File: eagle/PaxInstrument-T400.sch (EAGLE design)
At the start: 122 parts, among them IC1 MCP3424, U1 MCP9800, U3 MCP73831, U4 MIC5219-3.3V, U7 USD-SOCKETNEW, U8 NC7S32, X2 FH12-12S-0.5SH, Y1 RESONATORSMD

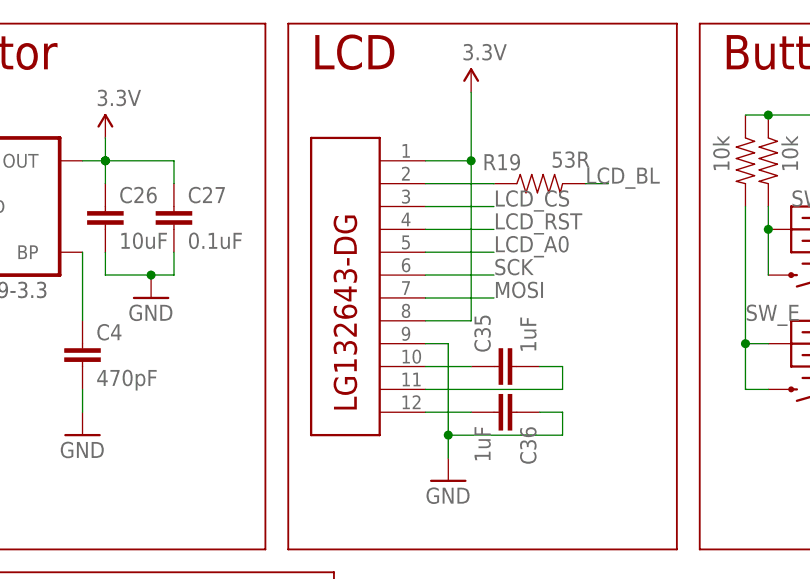
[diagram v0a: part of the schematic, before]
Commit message: - Moved switches a little
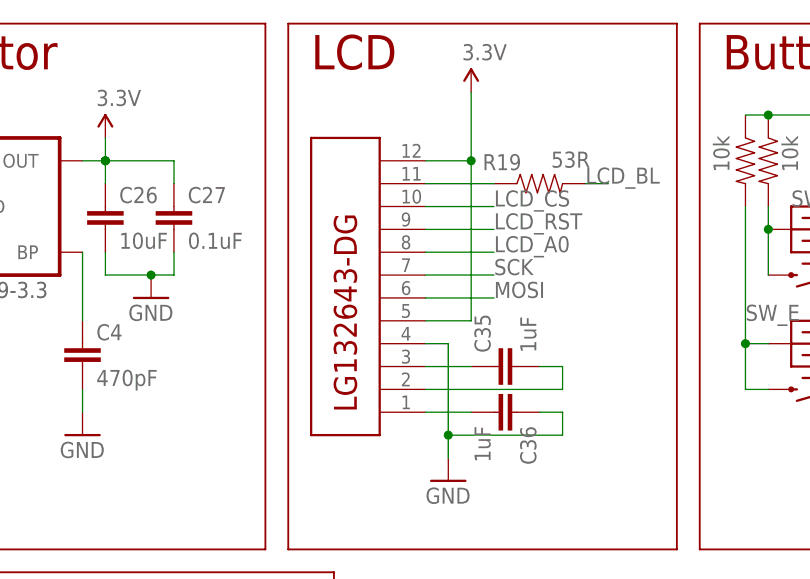
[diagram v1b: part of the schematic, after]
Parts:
- removed X2: FH12-12S-0.5SH, charlespax:FH12-12S-0.5SH
- added X1: FH12-12S-0.5SH, charlespax:FH12-12S-0.5SH
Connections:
- net 3.3V: now also X1.P$12, X1.P$5; no longer X2.P$1, X2.P$8
- net GND: now also X1.P$4; no longer X2.P$9
- net LCD_A0: now also X1.P$8; no longer X2.P$5
- net LCD_CS: now also X1.P$10; no longer X2.P$3
- net LCD_RST: now also X1.P$9; no longer X2.P$4
- net MOSI: now also X1.P$6; no longer X2.P$7
- net N$37: now also X1.P$3; no longer X2.P$10
- net N$38: now also X1.P$2; no longer X2.P$11
- net N$39: now also X1.P$1; no longer X2.P$12
- net N$4: now also X1.P$11; no longer X2.P$2
- net SCK: now also X1.P$7; no longer X2.P$6
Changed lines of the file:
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@@
 </part>
 <part name="GND17" library="SparkFun-Aesthetics" deviceset="GND" device=""/>
-<part name="X2" library="charlespax" deviceset="FH12-12S-0.5S" device="H">
-<attribute name="OC_DIGIKEY" value="HFJ112TR-ND"/>
-</part>
 <part name="P+4" library="SparkFun" deviceset="3.3V" device=""/>
 <part name="R19" library="SparkFun-Passives" deviceset="RESISTOR" device="0805-RES" value="53R"/>
@@
 <part name="GND20" library="SparkFun-Aesthetics" deviceset="GND" device=""/>
 <part name="P+8" library="SparkFun" deviceset="3.3V" device=""/>
+<part name="X1" library="charlespax" deviceset="FH12-12S-0.5S" device="H">
+<attribute name="OC_DIGIKEY" value="HFJ112TR-ND"/>
+</part>
 </parts>
 <sheets>
@@
 </instance>
 <instance part="GND17" gate="1" x="304.8" y="203.2"/>
-<instance part="X2" gate="G$1" x="297.18" y="210.82">
-<attribute name="OC_DIGIKEY" x="297.18" y="210.82" size="1.778" layer="96" display="off"/>
-</instance>
 <instance part="P+4" gate="G$1" x="307.34" y="246.38"/>
 <instance part="R19" gate="G$1" x="314.96" y="236.22" smashed="yes">
@@
 <instance part="GND20" gate="1" x="226.06" y="160.02"/>
 <instance part="P+8" gate="G$1" x="215.9" y="185.42"/>
+<instance part="X1" gate="G$1" x="297.18" y="238.76" rot="MR180">
+<attribute name="OC_DIGIKEY" x="297.18" y="238.76" size="1.778" layer="96" rot="MR180" display="off"/>
+</instance>
 </instances>
 <busses>
@@
 </segment>
 <segment>
-<pinref part="X2" gate="G$1" pin="P$8"/>
 <pinref part="P+4" gate="G$1" pin="3.3V"/>
 <wire x1="302.26" y1="220.98" x2="307.34" y2="220.98" width="0.1524" layer="91"/>
 <wire x1="307.34" y1="220.98" x2="307.34" y2="238.76" width="0.1524" layer="91"/>
-<pinref part="X2" gate="G$1" pin="P$1"/>
 <wire x1="307.34" y1="238.76" x2="307.34" y2="246.38" width="0.1524" layer="91"/>
 <wire x1="302.26" y1="238.76" x2="307.34" y2="238.76" width="0.1524" layer="91"/>
 <junction x="307.34" y="238.76"/>
+<pinref part="X1" gate="G$1" pin="P$5"/>
+<pinref part="X1" gate="G$1" pin="P$12"/>
 </segment>
 <segment>
@@
 <segment>
 <pinref part="GND17" gate="1" pin="GND"/>
-<pinref part="X2" gate="G$1" pin="P$9"/>
 <wire x1="304.8" y1="218.44" x2="304.8" y2="208.28" width="0.1524" layer="91"/>
 <wire x1="304.8" y1="208.28" x2="304.8" y2="205.74" width="0.1524" layer="91"/>
@@
 <wire x1="317.5" y1="208.28" x2="304.8" y2="208.28" width="0.1524" layer="91"/>
 <junction x="304.8" y="208.28"/>
+<pinref part="X1" gate="G$1" pin="P$4"/>
 </segment>
 <segment>
@@
 </segment>
 <segment>
-<pinref part="X2" gate="G$1" pin="P$7"/>
 <wire x1="302.26" y1="223.52" x2="309.88" y2="223.52" width="0.1524" layer="91"/>
 <label x="309.88" y="223.52" size="1.778" layer="95"/>
+<pinref part="X1" gate="G$1" pin="P$6"/>
 </segment>
 <segment>
@@
 </segment>
 <segment>
-<pinref part="X2" gate="G$1" pin="P$6"/>
 <wire x1="302.26" y1="226.06" x2="309.88" y2="226.06" width="0.1524" layer="91"/>
 <label x="309.88" y="226.06" size="1.778" layer="95"/>
+<pinref part="X1" gate="G$1" pin="P$7"/>
 </segment>
 <segment>
@@
 <net name="LCD_A0" class="0">
 <segment>
-<pinref part="X2" gate="G$1" pin="P$5"/>
 <wire x1="302.26" y1="228.6" x2="309.88" y2="228.6" width="0.1524" layer="91"/>
 <label x="309.88" y="228.6" size="1.778" layer="95"/>
+<pinref part="X1" gate="G$1" pin="P$8"/>
 </segment>
 <segment>
@@
 <net name="LCD_CS" class="0">
 <segment>
-<pinref part="X2" gate="G$1" pin="P$3"/>
 <wire x1="302.26" y1="233.68" x2="309.88" y2="233.68" width="0.1524" layer="91"/>
 <label x="309.88" y="233.68" size="1.778" layer="95"/>
+<pinref part="X1" gate="G$1" pin="P$10"/>
 </segment>
 <segment>
@@
 <net name="LCD_RST" class="0">
 <segment>
-<pinref part="X2" gate="G$1" pin="P$4"/>
 <wire x1="302.26" y1="231.14" x2="309.88" y2="231.14" width="0.1524" layer="91"/>
 <label x="309.88" y="231.14" size="1.778" layer="95"/>
+<pinref part="X1" gate="G$1" pin="P$9"/>
 </segment>
 <segment>
@@
 <net name="N$37" class="0">
 <segment>
-<pinref part="X2" gate="G$1" pin="P$10"/>
 <wire x1="302.26" y1="215.9" x2="307.34" y2="215.9" width="0.1524" layer="91"/>
 <pinref part="C35" gate="G$1" pin="1"/>
+<pinref part="X1" gate="G$1" pin="P$3"/>
 </segment>
 </net>
 <net name="N$38" class="0">
 <segment>
-<pinref part="X2" gate="G$1" pin="P$11"/>
 <pinref part="C35" gate="G$1" pin="2"/>
 <wire x1="314.96" y1="215.9" x2="317.5" y2="215.9" width="0.1524" layer="91"/>
 <wire x1="317.5" y1="215.9" x2="317.5" y2="213.36" width="0.1524" layer="91"/>
 <wire x1="317.5" y1="213.36" x2="302.26" y2="213.36" width="0.1524" layer="91"/>
+<pinref part="X1" gate="G$1" pin="P$2"/>
 </segment>
 </net>
 <net name="N$39" class="0">
 <segment>
-<pinref part="X2" gate="G$1" pin="P$12"/>
 <wire x1="302.26" y1="210.82" x2="307.34" y2="210.82" width="0.1524" layer="91"/>
 <pinref part="C36" gate="G$1" pin="2"/>
+<pinref part="X1" gate="G$1" pin="P$1"/>
 </segment>
 </net>
@@
 <net name="N$4" class="0">
 <segment>
-<pinref part="X2" gate="G$1" pin="P$2"/>
 <pinref part="R19" gate="G$1" pin="1"/>
 <wire x1="302.26" y1="236.22" x2="309.88" y2="236.22" width="0.1524" layer="91"/>
-</segment>
-</net>
+<pinref part="X1" gate="G$1" pin="P$11"/>
+</segment>
+</net>

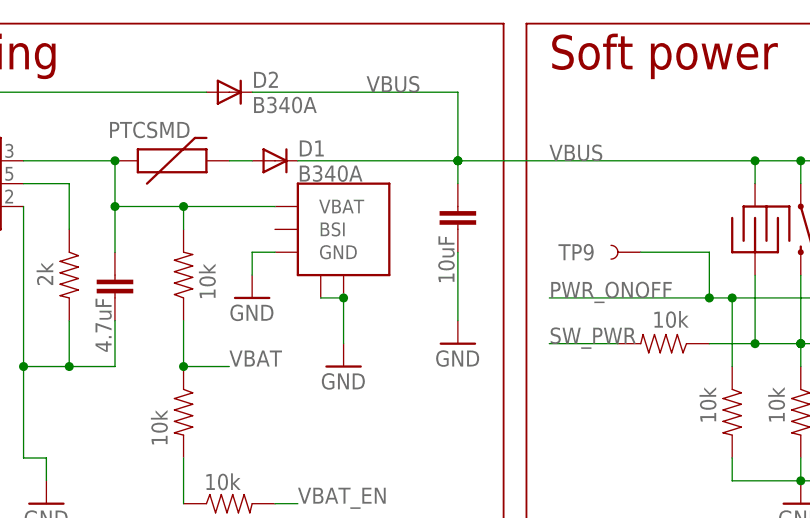
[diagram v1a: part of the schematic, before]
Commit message: - Still laying out board
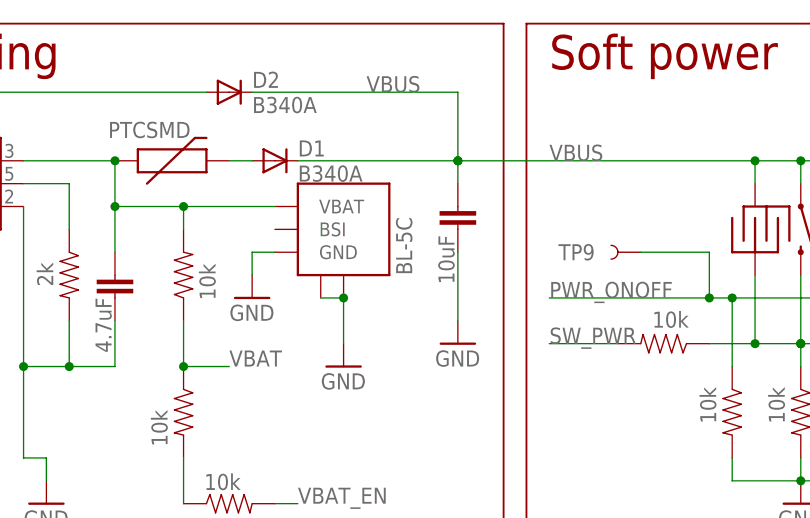
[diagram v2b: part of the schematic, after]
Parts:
- added U$6: BL-5C-OUTLINE, charlespax:BL-5C-OUTLINE
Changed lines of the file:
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@@
 <grid distance="0.1" unitdist="inch" unit="inch" style="lines" multiple="1" display="no" altdistance="0.01" altunitdist="inch" altunit="inch"/>
 <layers>
-<layer number="1" name="Top" color="4" fill="1" visible="no" active="no"/>
-<layer number="2" name="Route2" color="1" fill="3" visible="no" active="no"/>
-<layer number="3" name="Route3" color="4" fill="3" visible="no" active="no"/>
-<layer number="14" name="Route14" color="1" fill="6" visible="no" active="no"/>
-<layer number="15" name="Route15" color="4" fill="6" visible="no" active="no"/>
-<layer number="16" name="Bottom" color="1" fill="1" visible="no" active="no"/>
-<layer number="17" name="Pads" color="2" fill="1" visible="no" active="no"/>
-<layer number="18" name="Vias" color="2" fill="1" visible="no" active="no"/>
-<layer number="19" name="Unrouted" color="6" fill="1" visible="no" active="no"/>
-<layer number="20" name="Dimension" color="15" fill="1" visible="no" active="no"/>
-<layer number="21" name="tPlace" color="16" fill="1" visible="no" active="no"/>
-<layer number="22" name="bPlace" color="14" fill="1" visible="no" active="no"/>
-<layer number="23" name="tOrigins" color="15" fill="1" visible="no" active="no"/>
-<layer number="24" name="bOrigins" color="15" fill="1" visible="no" active="no"/>
-<layer number="25" name="tNames" color="7" fill="1" visible="no" active="no"/>
-<layer number="26" name="bNames" color="7" fill="1" visible="no" active="no"/>
-<layer number="27" name="tValues" color="7" fill="1" visible="no" active="no"/>
-<layer number="28" name="bValues" color="7" fill="1" visible="no" active="no"/>
+<layer number="1" name="Top" color="4" fill="1" visible="yes" active="no"/>
+<layer number="2" name="Route2" color="1" fill="3" visible="yes" active="no"/>
+<layer number="3" name="Route3" color="4" fill="3" visible="yes" active="no"/>
+<layer number="14" name="Route14" color="1" fill="6" visible="yes" active="no"/>
+<layer number="15" name="Route15" color="4" fill="6" visible="yes" active="no"/>
+<layer number="16" name="Bottom" color="1" fill="1" visible="yes" active="no"/>
+<layer number="17" name="Pads" color="2" fill="1" visible="yes" active="no"/>
+<layer number="18" name="Vias" color="2" fill="1" visible="yes" active="no"/>
+<layer number="19" name="Unrouted" color="6" fill="1" visible="yes" active="no"/>
+<layer number="20" name="Dimension" color="15" fill="1" visible="yes" active="no"/>
+<layer number="21" name="tPlace" color="16" fill="1" visible="yes" active="no"/>
+<layer number="22" name="bPlace" color="14" fill="1" visible="yes" active="no"/>
+<layer number="23" name="tOrigins" color="15" fill="1" visible="yes" active="no"/>
+<layer number="24" name="bOrigins" color="15" fill="1" visible="yes" active="no"/>
+<layer number="25" name="tNames" color="7" fill="1" visible="yes" active="no"/>
+<layer number="26" name="bNames" color="7" fill="1" visible="yes" active="no"/>
+<layer number="27" name="tValues" color="7" fill="1" visible="yes" active="no"/>
+<layer number="28" name="bValues" color="7" fill="1" visible="yes" active="no"/>
 <layer number="29" name="tStop" color="7" fill="3" visible="no" active="no"/>
 <layer number="30" name="bStop" color="7" fill="6" visible="no" active="no"/>
@@
 <layer number="35" name="tGlue" color="7" fill="4" visible="no" active="no"/>
 <layer number="36" name="bGlue" color="7" fill="5" visible="no" active="no"/>
-<layer number="37" name="tTest" color="7" fill="1" visible="no" active="no"/>
-<layer number="38" name="bTest" color="7" fill="1" visible="no" active="no"/>
+<layer number="37" name="tTest" color="7" fill="1" visible="yes" active="no"/>
+<layer number="38" name="bTest" color="7" fill="1" visible="yes" active="no"/>
 <layer number="39" name="tKeepout" color="4" fill="11" visible="no" active="no"/>
 <layer number="40" name="bKeepout" color="1" fill="11" visible="no" active="no"/>
@@
 <layer number="44" name="Drills" color="7" fill="1" visible="no" active="no"/>
 <layer number="45" name="Holes" color="7" fill="1" visible="no" active="no"/>
-<layer number="46" name="Milling" color="3" fill="1" visible="no" active="no"/>
-<layer number="47" name="Measures" color="7" fill="1" visible="no" active="no"/>
-<layer number="48" name="Document" color="7" fill="1" visible="no" active="no"/>
-<layer number="49" name="Reference" color="7" fill="1" visible="no" active="no"/>
-<layer number="50" name="dxf" color="7" fill="1" visible="no" active="no"/>
-<layer number="51" name="tDocu" color="6" fill="1" visible="no" active="no"/>
-<layer number="52" name="bDocu" color="7" fill="1" visible="no" active="no"/>
-<layer number="53" name="tGND_GNDA" color="7" fill="9" visible="no" active="no"/>
-<layer number="54" name="bGND_GNDA" color="1" fill="9" visible="no" active="no"/>
-<layer number="56" name="wert" color="7" fill="1" visible="no" active="no"/>
+<layer number="46" name="Milling" color="3" fill="1" visible="yes" active="no"/>
+<layer number="47" name="Measures" color="7" fill="1" visible="yes" active="no"/>
+<layer number="48" name="Document" color="7" fill="1" visible="yes" active="no"/>
+<layer number="49" name="Reference" color="7" fill="1" visible="yes" active="no"/>
+<layer number="50" name="dxf" color="7" fill="1" visible="yes" active="no"/>
+<layer number="51" name="tDocu" color="6" fill="1" visible="yes" active="no"/>
+<layer number="52" name="bDocu" color="7" fill="1" visible="yes" active="no"/>
+<layer number="53" name="tGND_GNDA" color="7" fill="9" visible="yes" active="no"/>
+<layer number="54" name="bGND_GNDA" color="1" fill="9" visible="yes" active="no"/>
+<layer number="56" name="wert" color="7" fill="1" visible="yes" active="no"/>
 <layer number="91" name="Nets" color="2" fill="1" visible="yes" active="yes"/>
 <layer number="92" name="Busses" color="1" fill="1" visible="yes" active="yes"/>
@@
 <attribute name="OC_DIGIKEY" value="HFJ112TR-ND"/>
 </part>
+<part name="U$6" library="charlespax" deviceset="BL-5C-OUTLINE" device=""/>
 </parts>
 <sheets>
@@
 <attribute name="OC_DIGIKEY" x="297.18" y="238.76" size="1.778" layer="96" rot="MR180" display="off"/>
 </instance>
+<instance part="U$6" gate="G$1" x="144.78" y="226.06" rot="R90"/>
 </instances>
 <busses>

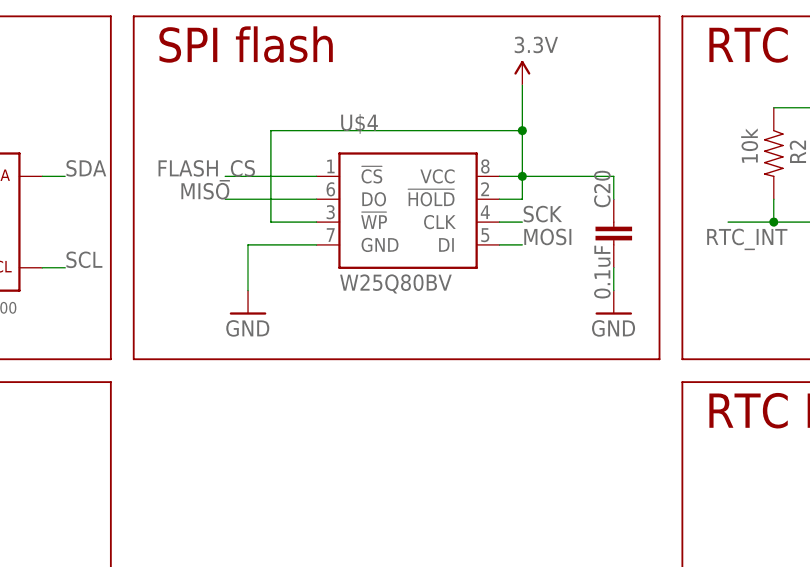
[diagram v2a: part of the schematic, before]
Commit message: - updated flash chip
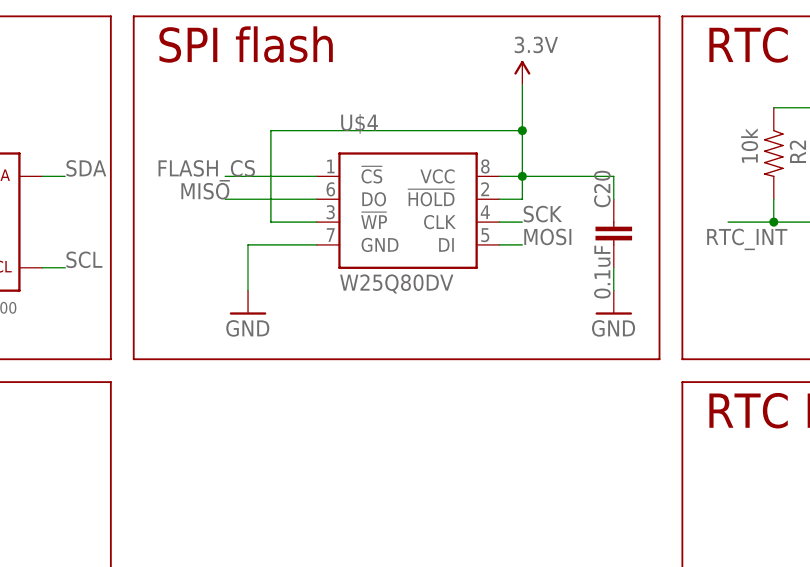
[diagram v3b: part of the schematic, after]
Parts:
- U$4: value W25Q80BV -> W25Q80DV
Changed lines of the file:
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@@
 <?xml version="1.0" encoding="utf-8"?>
 <!DOCTYPE eagle SYSTEM "eagle.dtd">
-<eagle version="6.6.0">
+<eagle version="6.5.0">
 <drawing>
 <settings>
@@
 </part>
 <part name="GND15" library="SparkFun-Aesthetics" deviceset="GND" device=""/>
-<part name="U$4" library="charlespax" deviceset="W25Q80BV" device="" value="W25Q80BV"/>
+<part name="U$4" library="charlespax" deviceset="W25Q80BV" device="" value="W25Q80DV"/>
 <part name="C20" library="SparkFun-Passives" deviceset="CAP" device="0805" value="0.1uF">
 <attribute name="MPN" value="CL10B104KO8NNNC"/>
